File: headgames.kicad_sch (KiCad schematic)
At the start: 49 parts, among them J1 9V BATTERY IN, J2 ELECTRODES, U1 LM358N INVENTORY, U2 LM324N INVENTORY, U3 LM386

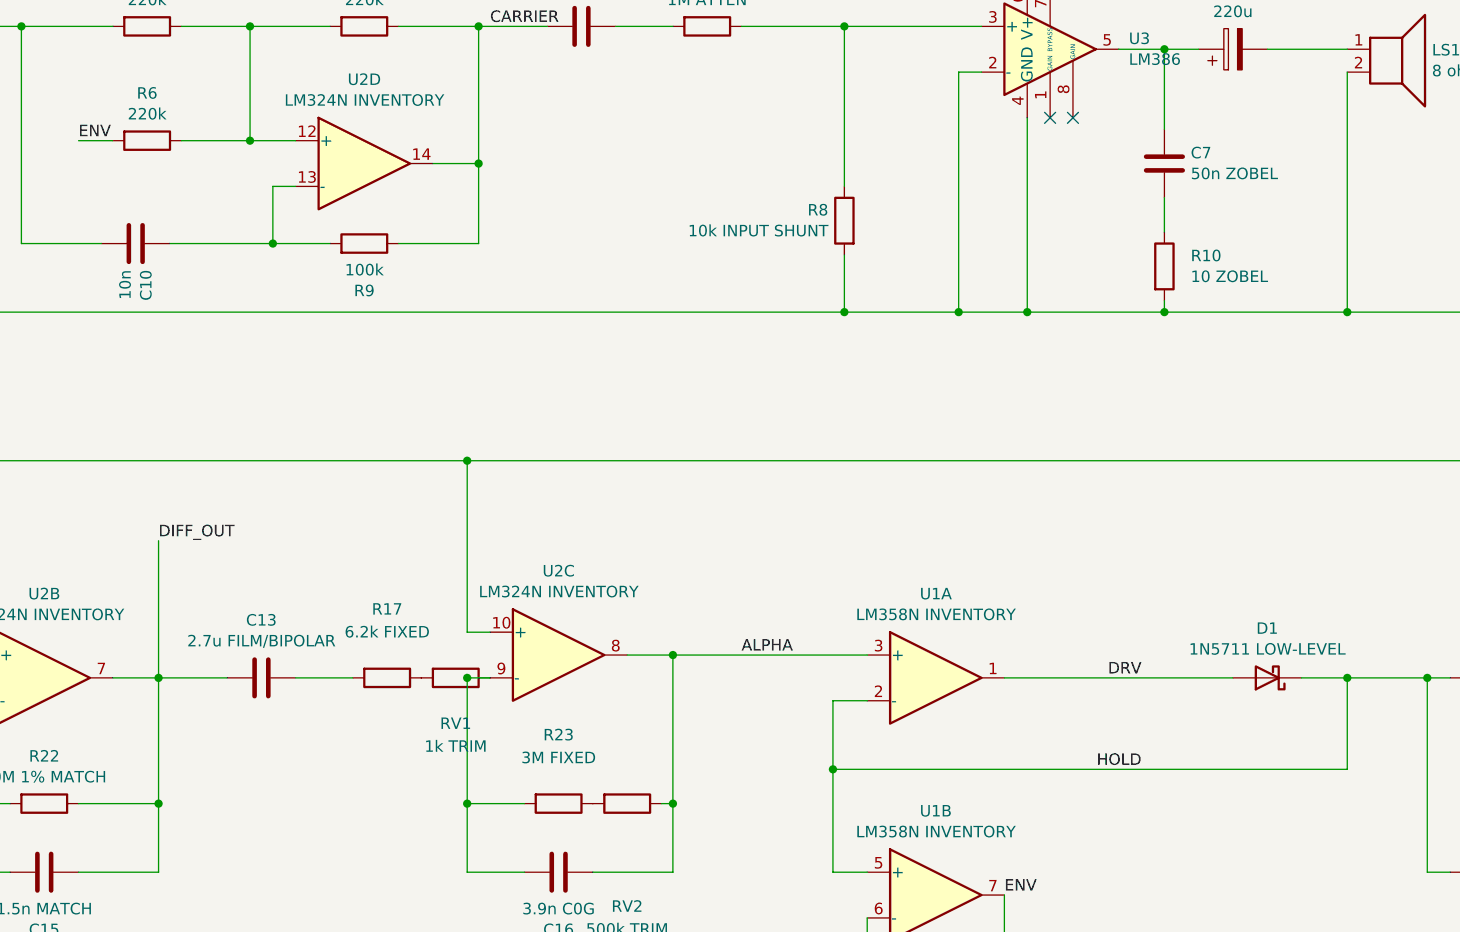
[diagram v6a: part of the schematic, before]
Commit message: Normalize adjustable filter parts to common values
Replace the difficult-to-source 2.7 uF alpha high-pass capacitor with a common 2.2 uF film or bipolar value and compensate with an 8.2 kOhm fixed resistor. Together with the existing 1 kOhm trim this preserves a bounded approximately 7.86-8.82 Hz high-pass adjustment range.

Replace the 3 MOhm low-pass resistor with the readily available 3.3 MOhm value. Retaining the 500 kOhm trim provides an approximately 10.74-12.37 Hz low-pass adjustment range that remains wholly above the maximum high-pass corner.

Normalize the LM386 output stabilization capacitor from nominal 50 nF to standard 47 nF while retaining the 10 Ohm series resistor. Update the authoritative architecture summary and durable engineering assertions to encode the new values and mathematically bounded ranges.
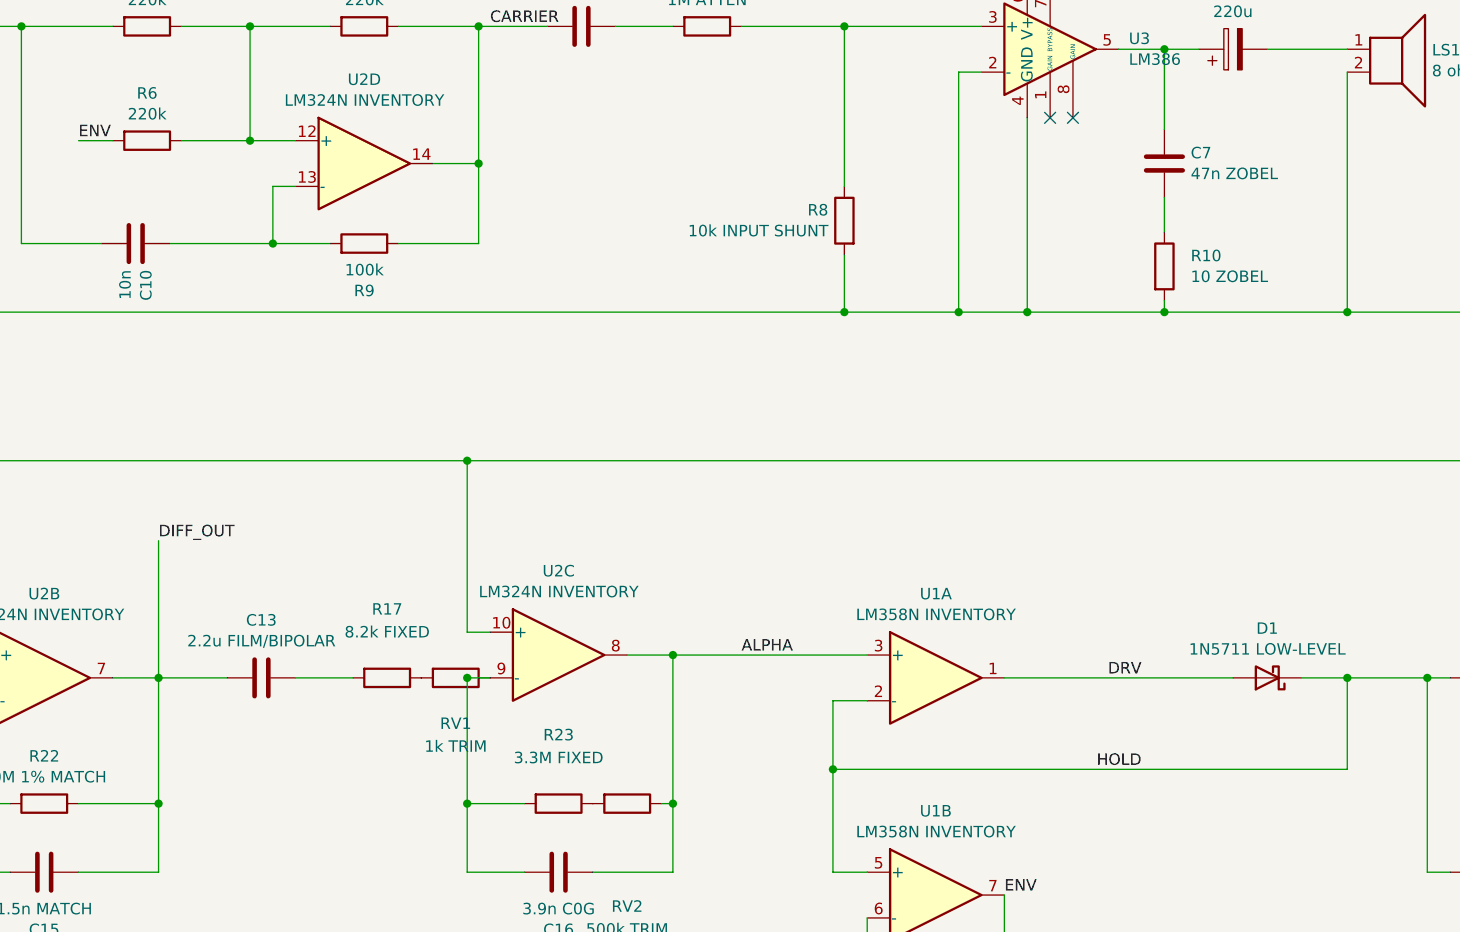
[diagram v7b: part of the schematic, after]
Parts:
- C13: value 2.7u FILM/BIPOLAR -> 2.2u FILM/BIPOLAR
- C7: value 50n ZOBEL -> 47n ZOBEL
- R17: value 6.2k FIXED -> 8.2k FIXED
- R23: value 3M FIXED -> 3.3M FIXED
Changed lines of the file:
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@@
 			)
 		)
-		(property "Value" "2.7u FILM/BIPOLAR"
+		(property "Value" "2.2u FILM/BIPOLAR"
 			(at 177.8 144.5006 90)
 			(effects
@@
 			)
 		)
-		(property "Value" "6.2k FIXED"
+		(property "Value" "8.2k FIXED"
 			(at 191.77 143.51 90)
 			(effects
@@
 			)
 		)
-		(property "Value" "3M FIXED"
+		(property "Value" "3.3M FIXED"
 			(at 210.82 157.48 90)
 			(effects
@@
 			)
 		)
-		(property "Value" "50n ZOBEL"
+		(property "Value" "47n ZOBEL"
 			(at 281.051 92.583 0)
 			(effects

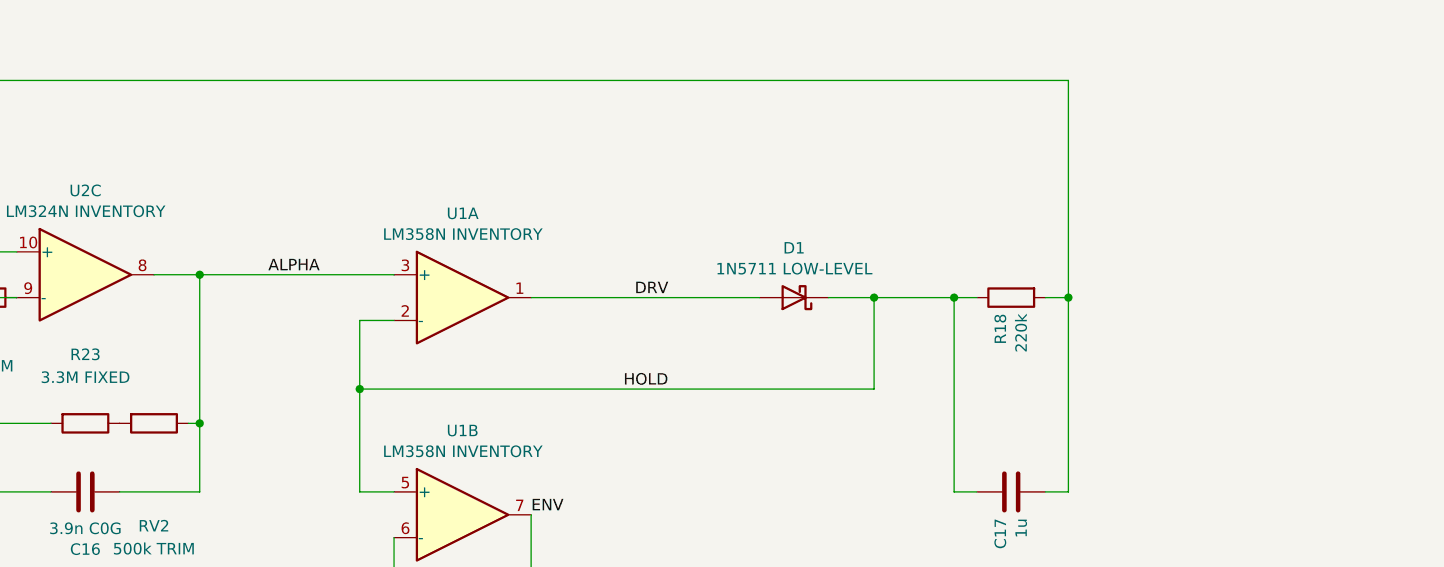
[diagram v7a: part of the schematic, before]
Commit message: Normalize the precision detector diode to 1N4148
Replace the specialized 1N5711 low-level Schottky with the ubiquitous 1N4148 small-signal silicon diode. D1 remains inside the LM358 precision-detector feedback loop, so the amplifier compensates the higher silicon forward drop rather than imposing it as an envelope threshold.

Prefer the 1N4148's low reverse leakage for the held envelope node. This keeps the detector release primarily controlled by the intentional 220 kOhm and 1 uF network instead of allowing a generic Schottky's leakage to become a significant parallel discharge path.

Update the schematic description, architectural invariant, and durable component assertion. Preserve the warning against generic power Schottky substitutions, which have unsuitable leakage and capacitance despite their superficially lower forward voltage.
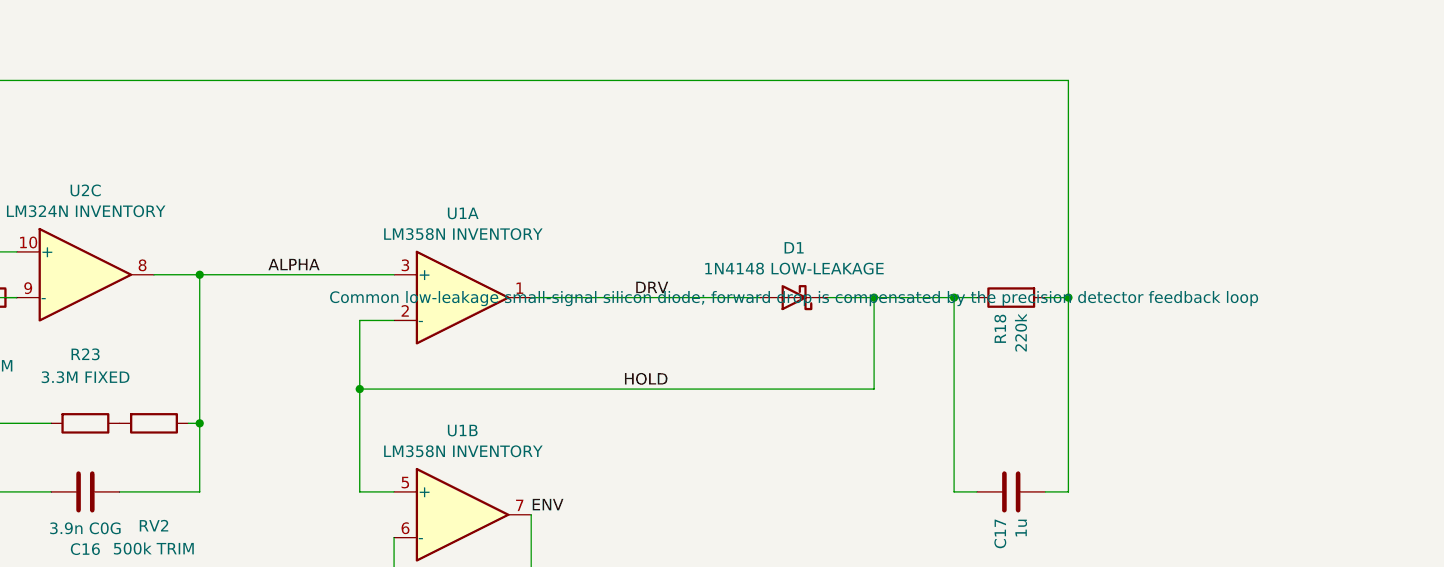
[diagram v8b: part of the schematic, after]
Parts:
- D1: value 1N5711 LOW-LEVEL -> 1N4148 LOW-LEAKAGE
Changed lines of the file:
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@@
 			)
 		)
-		(property "Value" "1N5711 LOW-LEVEL"
+		(property "Value" "1N4148 LOW-LEAKAGE"
 			(at 289.56 145.415 0)
 			(effects
@@
 			)
 		)
-		(property "Description" ""
+		(property "Description" "Common low-leakage small-signal silicon diode; forward drop is compensated by the precision detector feedback loop"
 			(at 289.56 148.59 0)
 			(effects
